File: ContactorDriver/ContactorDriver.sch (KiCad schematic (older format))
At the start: 17 parts, among them J1 PowerConn, J2 DashboardConn, J3 ContactorConn, Q1 CSD18511KTT

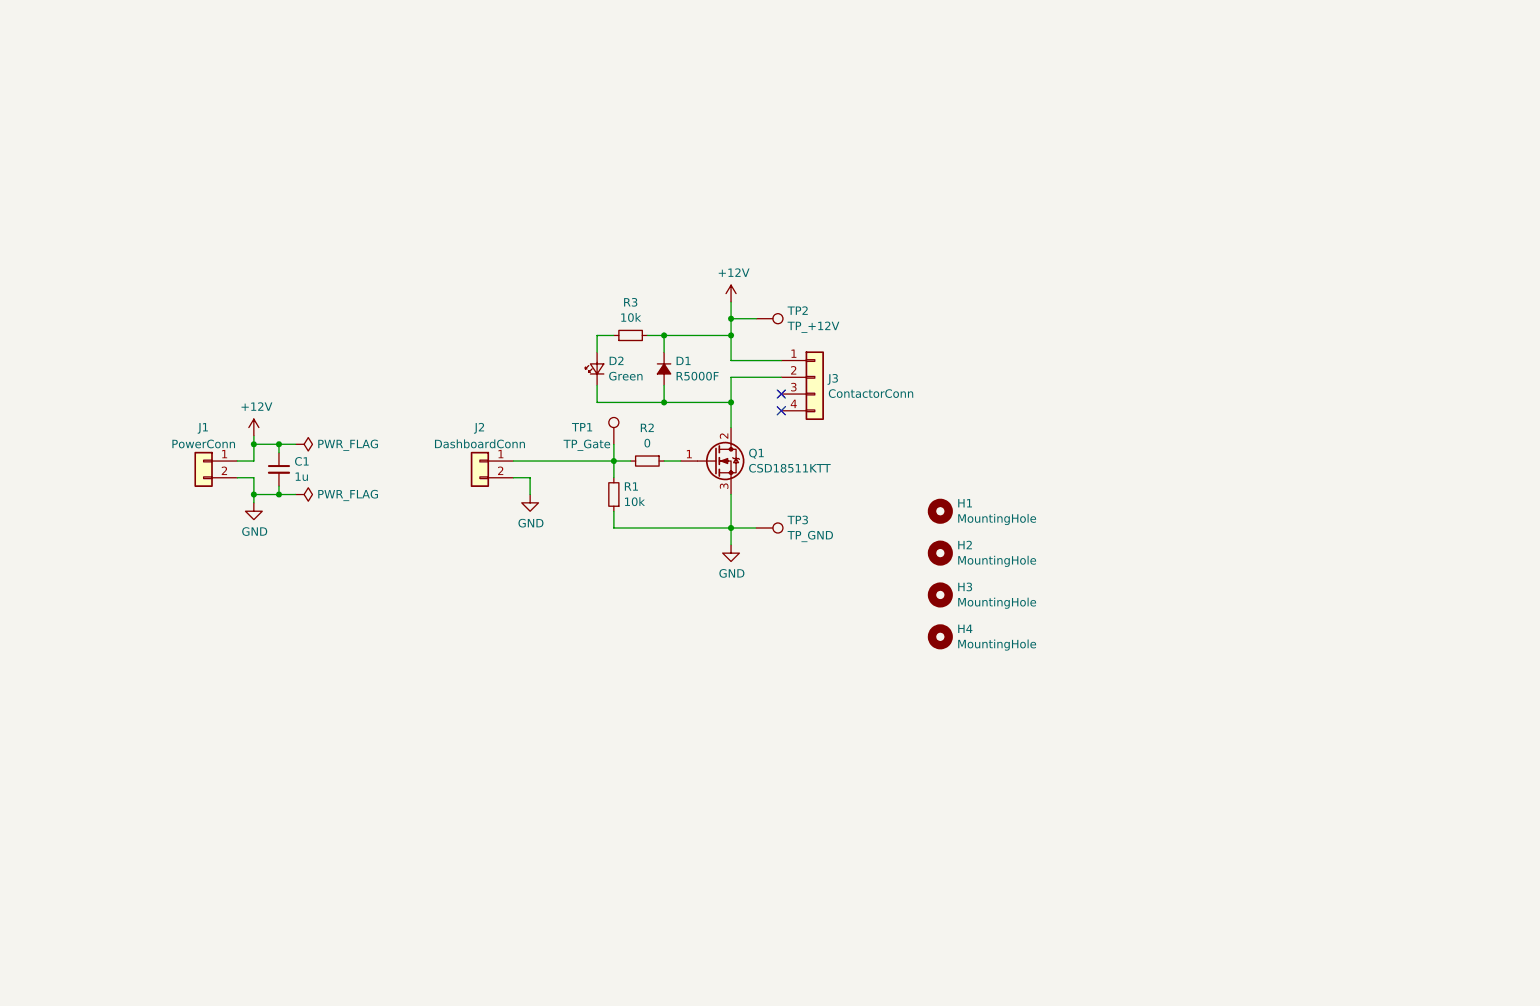
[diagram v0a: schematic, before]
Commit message: Adds BPS master board with no temperature brd electronics and ContactorDriver for dashboard to control.
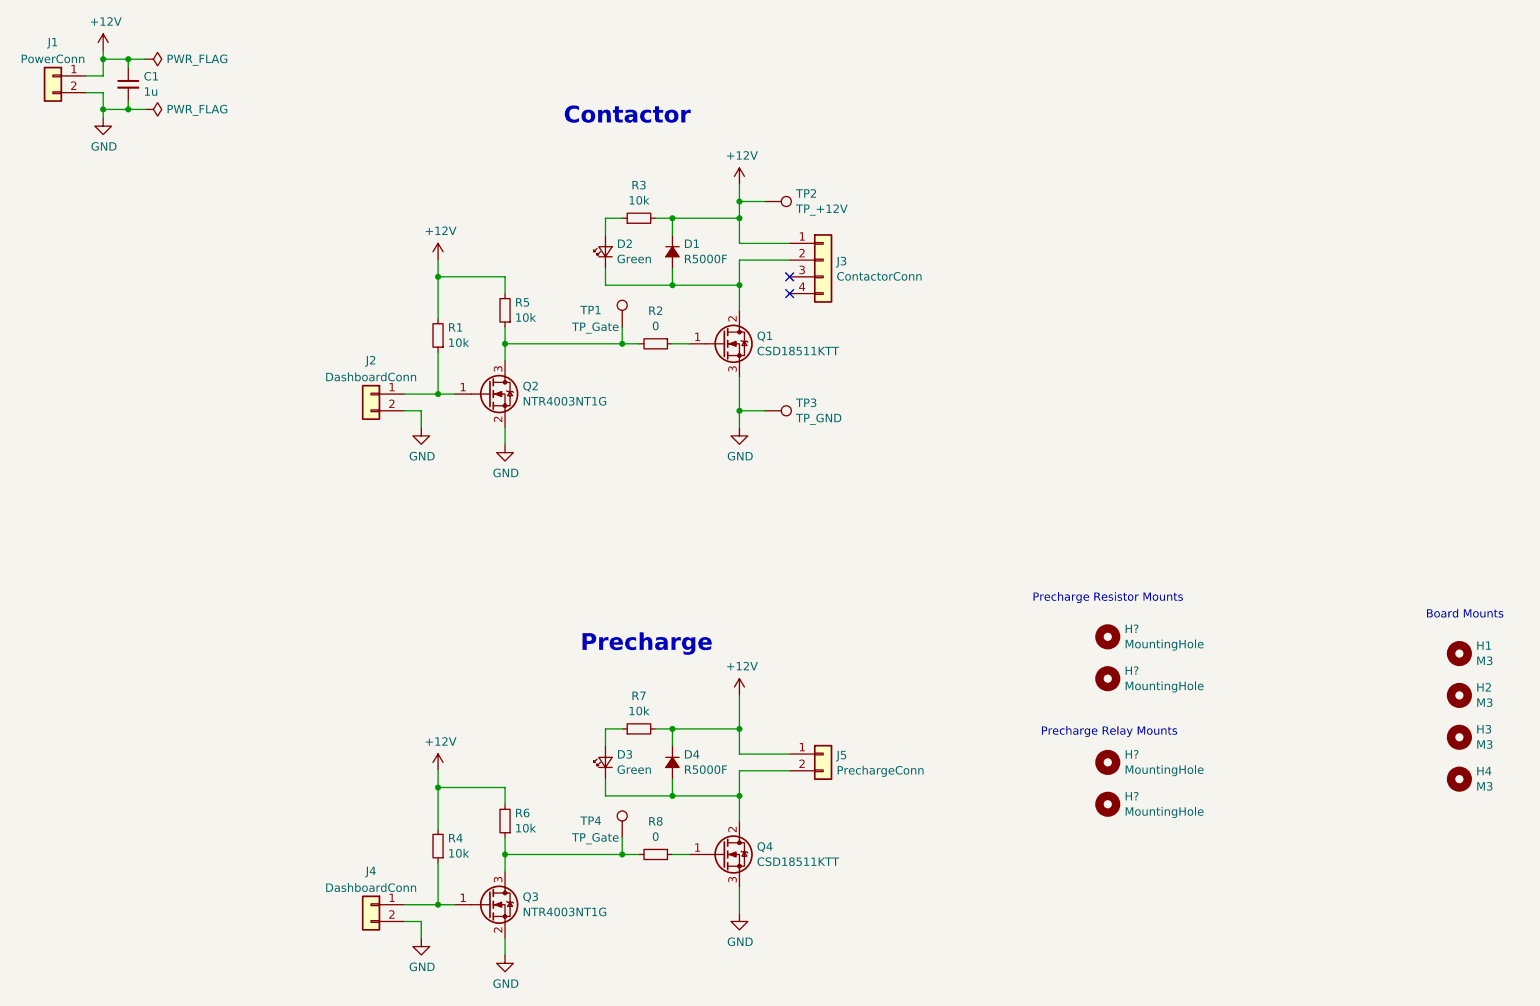
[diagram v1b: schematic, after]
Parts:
- added D3: Green, LED_SMD:LED_0805_2012Metric_Pad1.15x1.40mm_HandSolder, symbol Device:LED_Small
- added D4: R5000F, Diode_THT:D_DO-15_P10.16mm_Horizontal, symbol Device:D_Small_ALT
- added H? (x4): MountingHole, symbol Mechanical:MountingHole
- added J4: DashboardConn, Connector_Molex:Molex_Micro-Fit_3.0_43650-0200_1x02_P3.00mm_Horizontal, symbol Connector_Generic:Conn_01x02
- added J5: PrechargeConn, Connector_Molex:Molex_Micro-Fit_3.0_43650-0215_1x02_P3.00mm_Vertical, symbol Connector_Generic:Conn_01x02
- added Q2, Q3: NTR4003NT1G, Package_TO_SOT_SMD:TSOT-23, symbol Device:Q_NMOS_GSD
- added Q4: CSD18511KTT, Package_TO_SOT_SMD:TO-263-3_TabPin2, symbol Device:Q_NMOS_GDS
- added R4, R5, R6, R7: 10k, Resistor_SMD:R_0805_2012Metric_Pad1.15x1.40mm_HandSolder, symbol Device:R_Small
- added R8: 0, Resistor_SMD:R_0805_2012Metric_Pad1.15x1.40mm_HandSolder, symbol Device:R_Small
- added TP4: TP_Gate, TestPoint:TestPoint_Keystone_5005-5009_Compact, symbol Connector:TestPoint
- H1, H2, H3, H4: value MountingHole -> M3
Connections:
- net +12V: now also R1.2, D4.1 (K), J5.1 (Pin_1), R4.2, R5.2, R6.2, R7.2
- net GND: now also J4.2 (Pin_2), Q2.2 (S), Q3.2 (S), Q4.3 (S); no longer R1.1
- net at R2.2, TP1.1: now also Q2.3 (D), R5.1; no longer J2.1 (Pin_1), R1.2
- new net: J2.1 (Pin_1), Q2.1 (G), R1.1
- new net: J4.1 (Pin_1), Q3.1 (G), R4.1
- new net: Q4.1 (G), R8.1
- new net: Q3.3 (D), R6.1, R8.2, TP4.1
- new net: D3.1 (K), D4.2 (A), J5.2 (Pin_2), Q4.2 (D)
- new net: D3.2 (A), R7.1
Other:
- note added: "Board Mounts"
- note added: "Contactor"
- note added: "Precharge"
- note added: "Precharge Relay Mounts"
- note added: "Precharge Resistor Mounts"
- moved on the sheet: C1, D1, D2, H1, H2, H3, H4, J1, J2, J3, Q1, R2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
